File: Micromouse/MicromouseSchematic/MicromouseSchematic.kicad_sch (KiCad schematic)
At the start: 28 parts, among them J10 Conn_01x06_MountingPin, J3 Conn_01x04_Pin, J4 Conn_01x02_Pin, J5 Conn_01x06_MountingPin, SW1 SW_Push, SW2 SW_Push, U5 STM32F746VETx, Y1 8MHz, Y2 32.768kHz

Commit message: Micromouse KiCad: STM32-centric routing; ERC errors 23→6; backups and gitignore
Body:
Connected almost all STM32 signals; ERC down to 6

Rework root schematic plus motor driver, IMU/magnetometer, IR sensor, and TOF
subsheets so the bulk of signals reach the STM32. KiCad ERC is not fully clean
yet, but major nets are in place: errors dropped from 23 to 6 while many
previously unconnected signals were wired.

Add 2026-04-08 schematic backup zips. Extend .gitignore for macOS .DS_Store
paths. Update MicromouseSchematic.kicad_prl.
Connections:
- net IMU_INT_1: now also U5.16 (PC1)
- net IMU_INT_2: now also U5.17 (PC2)
- net IR_POW_1: now also U5.1 (PE2)
- net IR_POW_2: now also U5.2 (PE3)
- net IR_POW_3: now also U5.3 (PE4)
- net IR_POW_4: now also U5.4 (PE5)
- net IR_REC_1: now also U5.18 (PC3)
- net IR_REC_2: now also U5.32 (PC4)
- net IR_REC_3: now also U5.22 (PA0)
- net IR_REC_4: now also U5.33 (PC5)
- net MAG_INT: now also U5.15 (PC0)
- net NSLEEP_HB_1: now also U5.37 (PE7)
- net NSLEEP_HB_2: now also U5.40 (PE10)
- net NSLEEP_LDO_1: now also U5.38 (PE8)
- net NSLEEP_LDO_2: now also U5.42 (PE12)
- net TOF_INT: now also U5.7 (PC13)
- net VISEN_1: now also U5.24 (PA2)
- net VISEN_2: now also U5.25 (PA3)
- net at C21.1: now also Y1.2; no longer U5.13 (PH1)
- net at C21.2: now also U5.13 (PH1); no longer Y1.2
- net MO1_IN1: now reaches U5.59 (PD12)
- net MO1_IN2: now reaches U5.60 (PD13)
- net MO2_IN1: now reaches U5.61 (PD14)
- net MO2_IN2: now reaches U5.62 (PD15)
- net I2C_SDA: now reaches U5.95 (PB8)
- net I2C_SCL: now reaches U5.96 (PB9)
- no-connect marks 70 -> 46
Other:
- sheet IMU and Magnetometer ports: added SCL (Common), SDA(Common); removed SCL (IMU), SCL(Magnetometer), SDA (IMU), SDA(Magnetometer)
- moved on the sheet: C19, C20, C21, R20, SW1, SW2, Y1

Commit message: Micromouse KiCad: MP6550 layout, schematic updates; ERC clean, warnings ~5–6
Relocate MP6550G-Z symbol and footprint trees from MicromouseSchematic into
Micromouse/MP6550G-Z and refresh sym-lib-table (portable ${KIPRJMOD} paths
where applicable, MP6550 at new location).

Update root schematic plus IMU, IR, motor driver, and TOF subsheets. KiCad
ERC: all errors resolved (previously 6 remaining after earlier bring-up).
Warnings reduced from roughly 35–40+ down to about 5–6.

Add MicromouseSchematic-2026-04-11_212024.zip backup.
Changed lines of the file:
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@@
 	)
 	(junction
-		(at 107.95 118.11)
-		(diameter 0)
-		(color 0 0 0 0)
-	)
-	(junction
 		(at 157.48 33.02)
 		(diameter 0)
@@
 	)
 	(junction
-		(at 107.95 115.57)
-		(diameter 0)
-		(color 0 0 0 0)
-	)
-	(junction
 		(at 83.82 33.02)
 		(diameter 0)
@@
 	(wire
 		(pts
-			(xy 107.95 120.65) (xy 107.95 118.11)
-		)
-		(stroke
-			(width 0)
-			(type default)
-		)
-	)
-	(wire
-		(pts
 			(xy 110.49 33.02) (xy 119.38 33.02)
 		)
@@
 	(wire
 		(pts
-			(xy 111.76 113.03) (xy 107.95 113.03)
-		)
-		(stroke
-			(width 0)
-			(type default)
-		)
-	)
-	(wire
-		(pts
 			(xy 50.8 100.33) (xy 53.34 100.33)
 		)
@@
 	(wire
 		(pts
-			(xy 107.95 113.03) (xy 107.95 115.57)
-		)
-		(stroke
-			(width 0)
-			(type default)
-		)
-	)
-	(wire
-		(pts
 			(xy 73.66 40.64) (xy 76.2 40.64)
 		)
@@
 	(wire
 		(pts
-			(xy 107.95 118.11) (xy 111.76 118.11)
+			(xy 99.06 118.11) (xy 101.6 118.11)
 		)
 		(stroke
@@
 	(wire
 		(pts
-			(xy 107.95 115.57) (xy 111.76 115.57)
-		)
-		(stroke
-			(width 0)
-			(type default)
-		)
-	)
-	(wire
-		(pts
 			(xy 119.38 33.02) (xy 128.27 33.02)
 		)
@@
 	(wire
 		(pts
-			(xy 111.76 120.65) (xy 107.95 120.65)
-		)
-		(stroke
-			(width 0)
-			(type default)
-		)
-	)
-	(wire
-		(pts
 			(xy 68.58 22.86) (xy 68.58 25.4)
 		)
@@
 	(wire
 		(pts
-			(xy 107.95 115.57) (xy 99.06 115.57)
+			(xy 99.06 115.57) (xy 101.6 115.57)
 		)
 		(stroke
@@
 	(wire
 		(pts
-			(xy 99.06 118.11) (xy 107.95 118.11)
-		)
-		(stroke
-			(width 0)
-			(type default)
-		)
-	)
-	(wire
-		(pts
 			(xy 16.51 59.69) (xy 16.51 60.96)
 		)
@@
 		)
 	)
+	(global_label "I2C_SDA"
+		(shape bidirectional)
+		(at 251.46 130.81 180)
+		(fields_autoplaced yes)
+		(effects
+			(font
+				(size 1.27 1.27)
+			)
+			(justify right)
+		)
+		(property "Intersheetrefs" "${INTERSHEET_REFS}"
+			(at 239.7435 130.81 0)
+			(effects
+				(font
+					(size 1.27 1.27)
+				)
+				(justify right)
+				(hide yes)
+			)
+		)
+	)
 	(global_label "3V3A"
 		(shape output)
@@
 		)
 	)
-	(global_label "TOF_I2C_SDA"
-		(shape bidirectional)
-		(at 251.46 130.81 180)
-		(fields_autoplaced yes)
-		(effects
-			(font
-				(size 1.27 1.27)
-			)
-			(justify right)
-		)
-		(property "Intersheetrefs" "${INTERSHEET_REFS}"
-			(at 235.3892 130.81 0)
-			(effects
-				(font
-					(size 1.27 1.27)
-				)
-				(justify right)
-				(hide yes)
-			)
-		)
-	)
 	(global_label "I2C_SDA"
 		(shape bidirectional)
@@
 		)
 	)
-	(global_label "TOF_I2C_SCL"
-		(shape bidirectional)
-		(at 251.46 135.89 180)
-		(fields_autoplaced yes)
-		(effects
-			(font
-				(size 1.27 1.27)
-			)
-			(justify right)
-		)
-		(property "Intersheetrefs" "${INTERSHEET_REFS}"
-			(at 235.4497 135.89 0)
-			(effects
-				(font
-					(size 1.27 1.27)
-				)
-				(justify right)
-				(hide yes)
-			)
-		)
-	)
 	(global_label "MO1_IN1"
 		(shape input)
@@
 	(global_label "I2C_SCL"
 		(shape bidirectional)
-		(at 111.76 118.11 0)
+		(at 101.6 118.11 0)
 		(fields_autoplaced yes)
 		(effects
@@
 		)
 		(property "Intersheetrefs" "${INTERSHEET_REFS}"
-			(at 123.416 118.11 0)
+			(at 113.256 118.11 0)
 			(effects
 				(font
@@
 		)
 	)
-	(global_label "TOF_I2C_SCL"
-		(shape bidirectional)
-		(at 111.76 120.65 0)
-		(fields_autoplaced yes)
-		(effects
-			(font
-				(size 1.27 1.27)
-			)
-			(justify left)
-		)
-		(property "Intersheetrefs" "${INTERSHEET_REFS}"
-			(at 127.7703 120.65 0)
-			(effects
-				(font
-					(size 1.27 1.27)
-				)
-				(justify left)
-				(hide yes)
-			)
-		)
-	)
 	(global_label "SWCLK"
 		(shape input)
@@
 	(global_label "I2C_SDA"
 		(shape bidirectional)
-		(at 111.76 113.03 0)
+		(at 101.6 115.57 0)
 		(fields_autoplaced yes)
 		(effects
@@
 		)
 		(property "Intersheetrefs" "${INTERSHEET_REFS}"
-			(at 123.4765 113.03 0)
+			(at 113.3165 115.57 0)
 			(effects
 				(font
@@
 		)
 	)
-	(global_label "SWCLK"
-		(shape input)
-		(at 25.4 171.45 0)
+	(global_label "I2C_SCL"
+		(shape bidirectional)
+		(at 251.46 135.89 180)
 		(fields_autoplaced yes)
 		(effects
@@
 				(size 1.27 1.27)
 			)
-			(justify left)
+			(justify right)
 		)
 		(property "Intersheetrefs" "${INTERSHEET_REFS}"
-			(at 34.6142 171.45 0)
+			(at 239.804 135.89 0)
 			(effects
 				(font
 					(size 1.27 1.27)
 				)
-				(justify left)
+				(justify right)
 				(hide yes)
 			)
 		)
 	)
-	(global_label "SWO"
+	(global_label "SWCLK"
 		(shape input)
-		(at 101.6 102.87 0)
+		(at 25.4 171.45 0)
 		(fields_autoplaced yes)
 		(effects
@@
 		)
 		(property "Intersheetrefs" "${INTERSHEET_REFS}"
-			(at 108.5766 102.87 0)
+			(at 34.6142 171.45 0)
 			(effects
 				(font
@@
 		)
 	)
-	(global_label "TOF_I2C_SDA"
-		(shape bidirectional)
-		(at 111.76 115.57 0)
+	(global_label "SWO"
+		(shape input)
+		(at 101.6 102.87 0)
 		(fields_autoplaced yes)
 		(effects
@@
 		)
 		(property "Intersheetrefs" "${INTERSHEET_REFS}"
-			(at 127.8308 115.57 0)
+			(at 108.5766 102.87 0)
 			(effects
 				(font

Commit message: udpated programming header
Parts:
- removed J3: Conn_01x04_Pin, symbol Connector:Conn_01x04_Pin
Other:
- moved on the sheet: J10

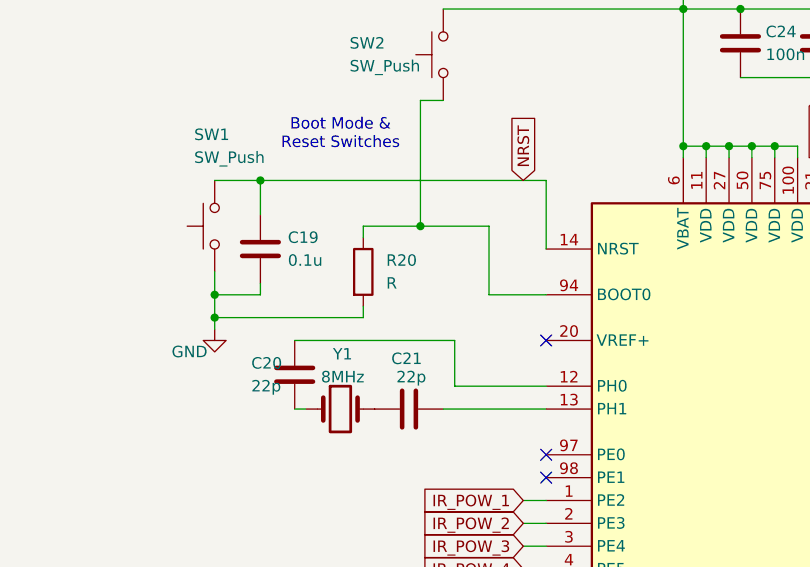
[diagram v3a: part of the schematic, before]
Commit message: assigned capacitor footprints. still have to figure out rest
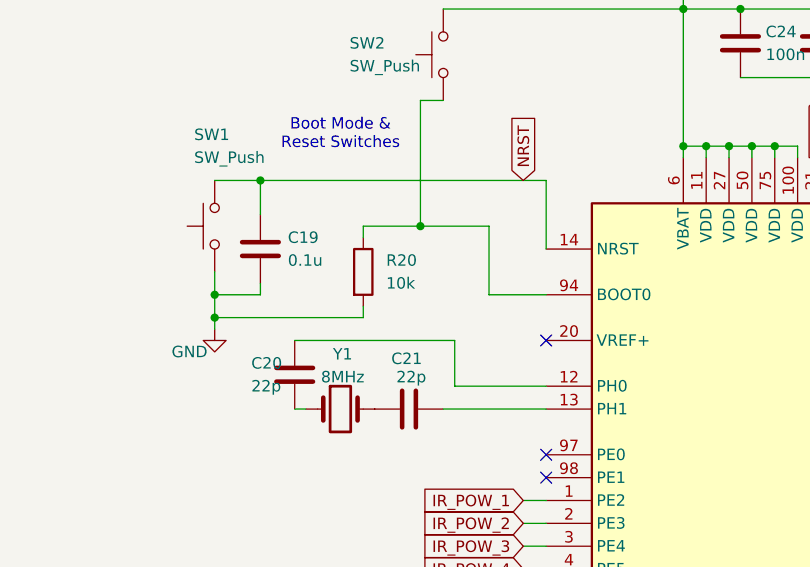
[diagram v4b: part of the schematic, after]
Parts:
- C19, C20, C21, C24, C25, C26, C27, C29, C30, C33, C35: footprint (none) -> Capacitor_SMD:C_0402_1005Metric
- C22, C23, C28, C31: footprint (none) -> Capacitor_SMD:C_0603_1608Metric
- C32: footprint (none) -> Capacitor_SMD:C_0805_2012Metric
- C34: footprint (none) -> Capacitor_SMD:C_0201_0603Metric
- R20: value R -> 10k; footprint (none) -> Resistor_SMD:R_0402_1005Metric
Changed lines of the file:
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@@
 			)
 		)
-		(property "Footprint" ""
+		(property "Footprint" "Capacitor_SMD:C_0603_1608Metric"
 			(at 51.7652 173.99 0)
 			(effects
@@
 			)
 		)
-		(property "Footprint" ""
+		(property "Footprint" "Capacitor_SMD:C_0402_1005Metric"
 			(at 22.5552 55.88 0)
 			(effects
@@
 			)
 		)
-		(property "Footprint" ""
+		(property "Footprint" "Capacitor_SMD:C_0402_1005Metric"
 			(at 26.3652 69.85 0)
 			(effects
@@
 			)
 		)
-		(property "Footprint" ""
+		(property "Footprint" "Capacitor_SMD:C_0402_1005Metric"
 			(at 75.8952 33.02 0)
 			(effects
@@
 			)
 		)
-		(property "Footprint" ""
+		(property "Footprint" "Capacitor_SMD:C_0402_1005Metric"
 			(at 41.91 68.8848 0)
 			(effects
@@
 			)
 		)
-		(property "Footprint" ""
+		(property "Footprint" "Capacitor_SMD:C_0402_1005Metric"
 			(at 169.8752 33.02 0)
 			(effects
@@
 			)
 		)
-		(property "Footprint" ""
+		(property "Footprint" "Capacitor_SMD:C_0603_1608Metric"
 			(at 42.8752 173.99 0)
 			(effects
@@
 			)
 		)
-		(property "Footprint" ""
+		(property "Footprint" "Capacitor_SMD:C_0603_1608Metric"
 			(at 107.6452 185.42 0)
 			(effects
@@
 			)
 		)
-		(property "Footprint" ""
+		(property "Footprint" "Capacitor_SMD:C_0402_1005Metric"
 			(at 120.3452 33.02 0)
 			(effects
@@
 			)
 		)
-		(property "Footprint" ""
+		(property "Footprint" "Capacitor_SMD:C_0402_1005Metric"
 			(at 84.7852 33.02 0)
 			(effects
@@
 			)
 		)
-		(property "Footprint" ""
+		(property "Footprint" "Capacitor_SMD:C_0402_1005Metric"
 			(at 111.4552 33.02 0)
 			(effects
@@
 			)
 		)
-		(property "Footprint" ""
+		(property "Footprint" "Capacitor_SMD:C_0805_2012Metric"
 			(at 129.2352 33.02 0)
 			(effects
@@
 			)
 		)
-		(property "Footprint" ""
+		(property "Footprint" "Capacitor_SMD:C_0402_1005Metric"
 			(at 139.3952 33.02 0)
 			(effects
@@
 			)
 		)
-		(property "Value" "R"
+		(property "Value" "10k"
 			(at 35.56 55.8799 0)
 			(effects
@@
 			)
 		)
-		(property "Footprint" ""
+		(property "Footprint" "Resistor_SMD:R_0402_1005Metric"
 			(at 31.242 54.61 90)
 			(effects
@@
 			)
 		)
-		(property "Footprint" ""
+		(property "Footprint" "Capacitor_SMD:C_0402_1005Metric"
 			(at 102.5652 33.02 0)
 			(effects
@@
 			)
 		)
-		(property "Footprint" ""
+		(property "Footprint" "Capacitor_SMD:C_0402_1005Metric"
 			(at 93.6752 33.02 0)
 			(effects
@@
 			)
 		)
-		(property "Footprint" ""
+		(property "Footprint" "Capacitor_SMD:C_0603_1608Metric"
 			(at 120.3452 185.42 0)
 			(effects
@@
 			)
 		)
-		(property "Footprint" ""
+		(property "Footprint" "Capacitor_SMD:C_0201_0603Metric"
 			(at 158.4452 33.02 0)
 			(effects

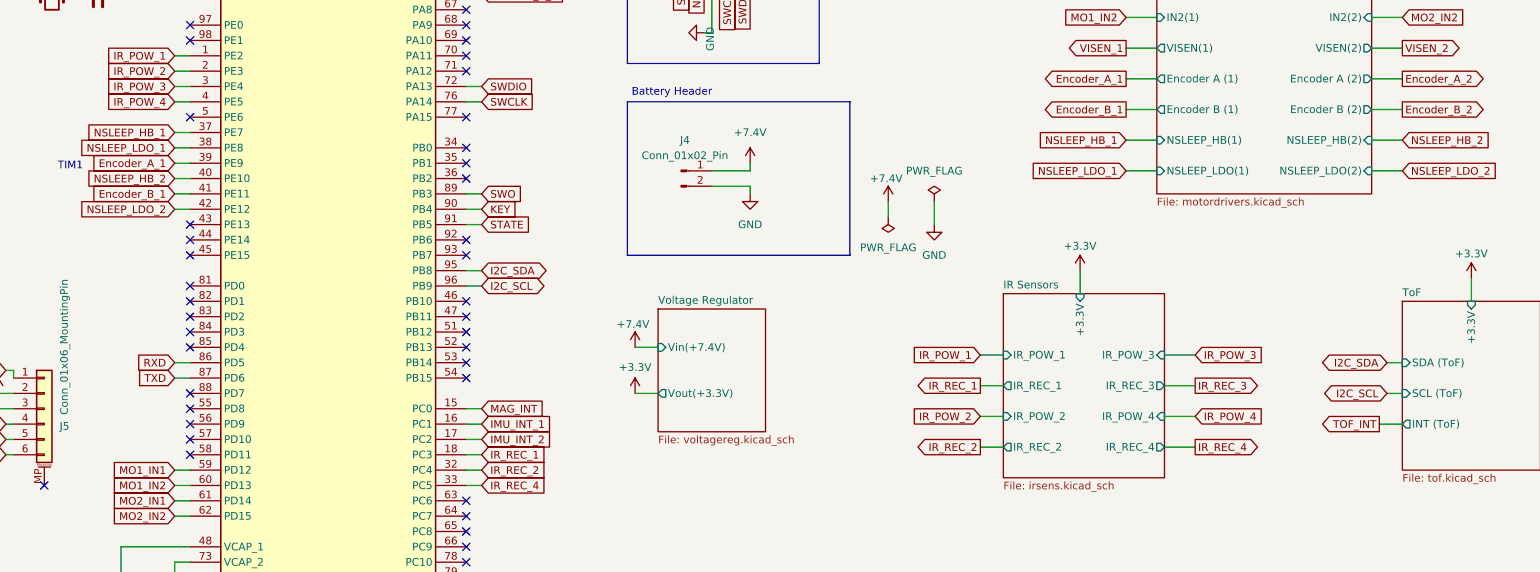
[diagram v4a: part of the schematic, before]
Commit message: Micromouse KiCad: VL53L4 TOF footprint/sym; fp-lib via KICAD_ADDITIONAL_FOOTPRINT
Add UltraLibrarian VL53L4CDV0DH-1 KiCad symbol and LGA12_STM footprint plus
vendor readme; register them in sym-lib-table and fp-lib-table.

Point MM footprint libraries at ${KICAD_ADDITIONAL_FOOTPRINT}/... for
portable paths; add MM_VL53L4CDV0DH-1.

Rework tof.kicad_sch (large cleanup vs embedded library bulk) and touch root
MicromouseSchematic.kicad_sch and MicromouseSchematic.kicad_pro for project
consistency.
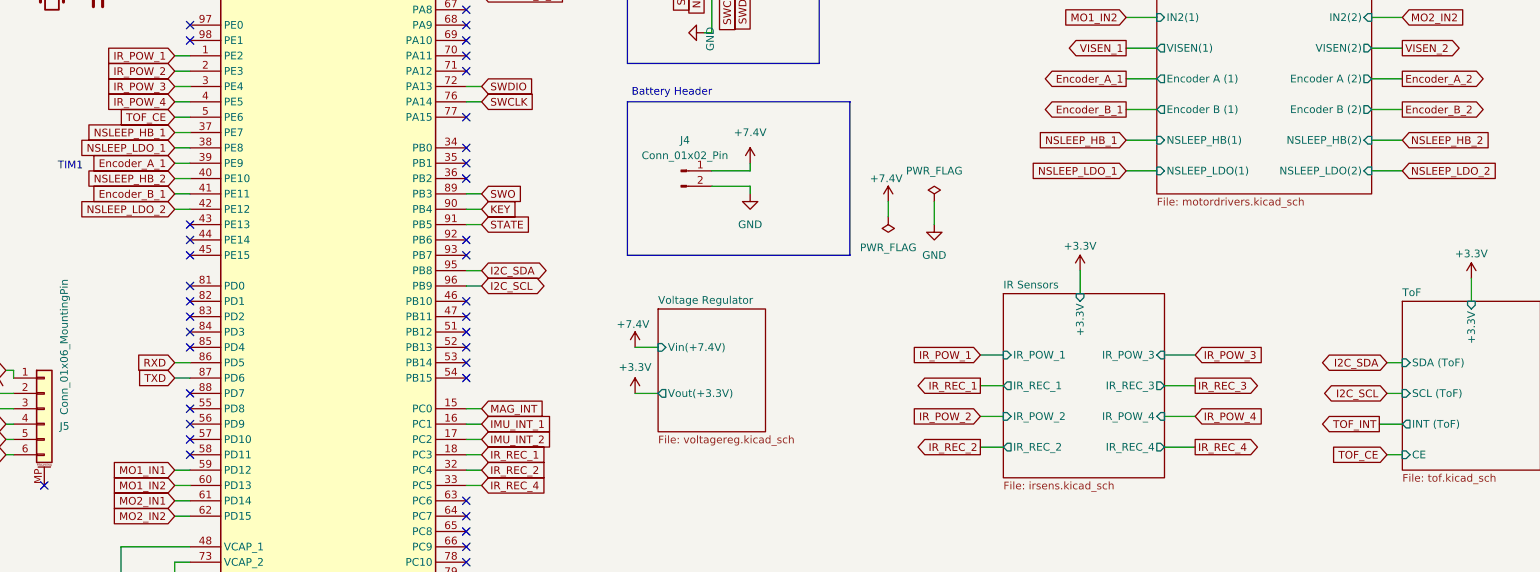
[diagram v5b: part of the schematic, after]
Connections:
- net TOF_CE: now reaches U5.5 (PE6)
- no-connect marks 46 -> 45
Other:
- sheet ToF ports: added CE; removed none
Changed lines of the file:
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@@
 	)
 	(no_connect
-		(at 53.34 90.17)
-	)
-	(no_connect
 		(at 99.06 72.39)
 	)
@@
 	(wire
 		(pts
+			(xy 50.8 90.17) (xy 53.34 90.17)
+		)
+		(stroke
+			(width 0)
+			(type default)
+		)
+	)
+	(wire
+		(pts
 			(xy 50.8 80.01) (xy 53.34 80.01)
 		)
@@
 	(wire
 		(pts
+			(xy 251.46 146.05) (xy 254 146.05)
+		)
+		(stroke
+			(width 0)
+			(type default)
+		)
+	)
+	(wire
+		(pts
 			(xy 78.74 187.96) (xy 78.74 186.69)
 		)
@@
 		)
 	)
+	(global_label "TOF_CE"
+		(shape input)
+		(at 50.8 90.17 180)
+		(fields_autoplaced yes)
+		(effects
+			(font
+				(size 1.27 1.27)
+			)
+			(justify right)
+		)
+		(property "Intersheetrefs" "${INTERSHEET_REFS}"
+			(at 41.0415 90.17 0)
+			(effects
+				(font
+					(size 1.27 1.27)
+				)
+				(justify right)
+				(hide yes)
+			)
+		)
+	)
 	(global_label "STATE"
 		(shape input)
@@
 		)
 	)
+	(global_label "TOF_CE"
+		(shape input)
+		(at 251.46 146.05 180)
+		(fields_autoplaced yes)
+		(effects
+			(font
+				(size 1.27 1.27)
+			)
+			(justify right)
+		)
+		(property "Intersheetrefs" "${INTERSHEET_REFS}"
+			(at 241.7015 146.05 0)
+			(effects
+				(font
+					(size 1.27 1.27)
+				)
+				(justify right)
+				(hide yes)
+			)
+		)
+	)
 	(global_label "NRST"
 		(shape input)
@@
 			)
 		)
+		(pin "CE" input
+			(at 254 146.05 180)
+			(effects
+				(font
+					(size 1.27 1.27)
+				)
+				(justify left)
+			)
+		)
